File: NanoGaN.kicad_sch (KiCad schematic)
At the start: 19 parts, among them J1 XT60-M, J2 XT60-M, J3 Phase_U, J4 Phase_V, J5 Phase_W

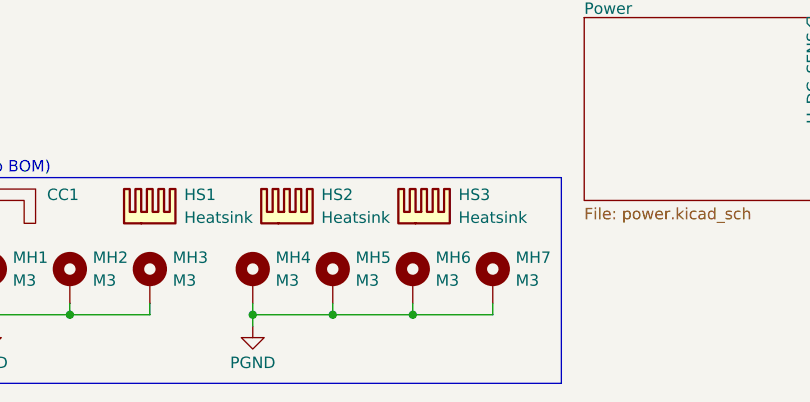
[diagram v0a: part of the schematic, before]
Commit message: new version of heatsink, channel and mounting holes
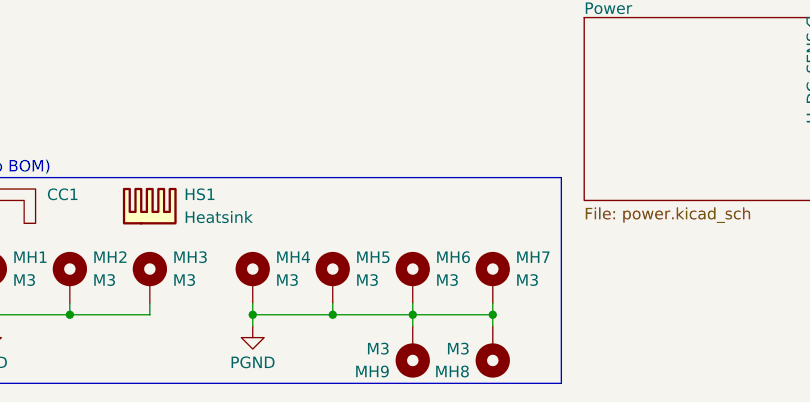
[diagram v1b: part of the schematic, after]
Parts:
- removed HS2, HS3: Heatsink, NanoGaN:HSB01-080808, symbol Mechanical:Heatsink
- added MH8, MH9: M3, MountingHole:MountingHole_3.2mm_M3_Pad_Via, symbol Mechanical:MountingHole_Pad
- HS1: footprint NanoGaN:HSB01-080808 -> NanoGaN:ICK_S
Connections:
- net PGND: now also MH8.1, MH9.1
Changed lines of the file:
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@@
+	)
+	(junction
+		(at 88.9 187.96)
+		(diameter 0)
+		(color 0 0 0 0)
 	)
 	(junction
@@
 	(wire
 		(pts
-			(xy 80.01 187.96) (xy 88.9 187.96)
-		)
-		(stroke
-			(width 0)
-			(type default)
-		)
-	)
-	(wire
-		(pts
 			(xy 88.9 54.61) (xy 99.06 54.61)
 		)
@@
 	(wire
 		(pts
+			(xy 88.9 187.96) (xy 80.01 187.96)
+		)
+		(stroke
+			(width 0)
+			(type default)
+		)
+	)
+	(wire
+		(pts
 			(xy 149.86 43.18) (xy 162.56 43.18)
 		)
@@
 	(wire
 		(pts
+			(xy 80.01 189.23) (xy 80.01 187.96)
+		)
+		(stroke
+			(width 0)
+			(type default)
+		)
+	)
+	(wire
+		(pts
 			(xy 88.9 24.13) (xy 99.06 24.13)
 		)
@@
 	(wire
 		(pts
+			(xy 88.9 189.23) (xy 88.9 187.96)
+		)
+		(stroke
+			(width 0)
+			(type default)
+		)
+	)
+	(wire
+		(pts
 			(xy 88.9 36.83) (xy 99.06 36.83)
 		)
@@
 			(width 0)
 			(type default)
+		)
+	)
+	(symbol
+		(lib_id "Mechanical:MountingHole_Pad")
+		(at 80.01 191.77 180)
+		(unit 1)
+		(exclude_from_sim yes)
+		(in_bom no)
+		(on_board yes)
+		(dnp no)
+		(fields_autoplaced yes)
+		(property "Reference" "MH9"
+			(at 77.47 194.3101 0)
+			(effects
+				(font
+					(size 1.27 1.27)
+				)
+				(justify left)
+			)
+		)
+		(property "Value" "M3"
+			(at 77.47 191.7701 0)
+			(effects
+				(font
+					(size 1.27 1.27)
+				)
+				(justify left)
+			)
+		)
+		(property "Footprint" "MountingHole:MountingHole_3.2mm_M3_Pad_Via"
+			(at 80.01 191.77 0)
+			(effects
+				(font
+					(size 1.27 1.27)
+				)
+				(hide yes)
+			)
+		)
+		(property "Datasheet" "~"
+			(at 80.01 191.77 0)
+			(effects
+				(font
+					(size 1.27 1.27)
+				)
+				(hide yes)
+			)
+		)
+		(property "Description" "Mounting Hole with connection"
+			(at 80.01 191.77 0)
+			(effects
+				(font
+					(size 1.27 1.27)
+				)
+				(hide yes)
+			)
+		)
+		(pin "1"
+		)
+		(instances
+			(project "NanoGaN"
+				(path "/aa8a494f-605e-4a00-9d3c-daec94709fcb"
+					(reference "MH9")
+					(unit 1)
+				)
+			)
 		)
 	)
@@
 	)
 	(symbol
-		(lib_id "Mechanical:Heatsink")
-		(at 66.04 177.8 0)
-		(unit 1)
-		(exclude_from_sim no)
-		(in_bom yes)
-		(on_board yes)
-		(dnp no)
-		(fields_autoplaced yes)
-		(property "Reference" "HS2"
-			(at 69.85 174.6249 0)
-			(effects
-				(font
-					(size 1.27 1.27)
-				)
-				(justify left)
-			)
-		)
-		(property "Value" "Heatsink"
-			(at 69.85 177.1649 0)
-			(effects
-				(font
-					(size 1.27 1.27)
-				)
-				(justify left)
-			)
-		)
-		(property "Footprint" "NanoGaN:HSB01-080808"
-			(at 66.3448 177.8 0)
-			(effects
-				(font
-					(size 1.27 1.27)
-				)
-				(hide yes)
-			)
-		)
-		(property "Datasheet" "~"
-			(at 66.3448 177.8 0)
-			(effects
-				(font
-					(size 1.27 1.27)
-				)
-				(hide yes)
-			)
-		)
-		(property "Description" "Heatsink"
-			(at 66.04 177.8 0)
-			(effects
-				(font
-					(size 1.27 1.27)
-				)
-				(hide yes)
-			)
-		)
-		(instances
-			(project "NanoGaN"
-				(path "/aa8a494f-605e-4a00-9d3c-daec94709fcb"
-					(reference "HS2")
-					(unit 1)
-				)
-			)
-		)
-	)
-	(symbol
-		(lib_id "Mechanical:Heatsink")
-		(at 81.28 177.8 0)
-		(unit 1)
-		(exclude_from_sim no)
-		(in_bom yes)
-		(on_board yes)
-		(dnp no)
-		(fields_autoplaced yes)
-		(property "Reference" "HS3"
-			(at 85.09 174.6249 0)
-			(effects
-				(font
-					(size 1.27 1.27)
-				)
-				(justify left)
-			)
-		)
-		(property "Value" "Heatsink"
-			(at 85.09 177.1649 0)
-			(effects
-				(font
-					(size 1.27 1.27)
-				)
-				(justify left)
-			)
-		)
-		(property "Footprint" "NanoGaN:HSB01-080808"
-			(at 81.5848 177.8 0)
-			(effects
-				(font
-					(size 1.27 1.27)
-				)
-				(hide yes)
-			)
-		)
-		(property "Datasheet" "~"
-			(at 81.5848 177.8 0)
-			(effects
-				(font
-					(size 1.27 1.27)
-				)
-				(hide yes)
-			)
-		)
-		(property "Description" "Heatsink"
-			(at 81.28 177.8 0)
-			(effects
-				(font
-					(size 1.27 1.27)
-				)
-				(hide yes)
-			)
-		)
-		(instances
-			(project "NanoGaN"
-				(path "/aa8a494f-605e-4a00-9d3c-daec94709fcb"
-					(reference "HS3")
-					(unit 1)
-				)
-			)
-		)
-	)
-	(symbol
 		(lib_id "Mechanical:MountingHole_Pad")
 		(at 62.23 184.15 0)
@@
 	)
 	(symbol
+		(lib_id "Mechanical:MountingHole_Pad")
+		(at 88.9 191.77 180)
+		(unit 1)
+		(exclude_from_sim yes)
+		(in_bom no)
+		(on_board yes)
+		(dnp no)
+		(fields_autoplaced yes)
+		(property "Reference" "MH8"
+			(at 86.36 194.3101 0)
+			(effects
+				(font
+					(size 1.27 1.27)
+				)
+				(justify left)
+			)
+		)
+		(property "Value" "M3"
+			(at 86.36 191.7701 0)
+			(effects
+				(font
+					(size 1.27 1.27)
+				)
+				(justify left)
+			)
+		)
+		(property "Footprint" "MountingHole:MountingHole_3.2mm_M3_Pad_Via"
+			(at 88.9 191.77 0)
+			(effects
+				(font
+					(size 1.27 1.27)
+				)
+				(hide yes)
+			)
+		)
+		(property "Datasheet" "~"
+			(at 88.9 191.77 0)
+			(effects
+				(font
+					(size 1.27 1.27)
+				)
+				(hide yes)
+			)
+		)
+		(property "Description" "Mounting Hole with connection"
+			(at 88.9 191.77 0)
+			(effects
+				(font
+					(size 1.27 1.27)
+				)
+				(hide yes)
+			)
+		)
+		(pin "1"
+		)
+		(instances
+			(project "NanoGaN"
+				(path "/aa8a494f-605e-4a00-9d3c-daec94709fcb"
+					(reference "MH8")
+					(unit 1)
+				)
+			)
+		)
+	)
+	(symbol
 		(lib_id "power:GND")
 		(at 33.02 189.23 0)
@@
 		(on_board yes)
 		(dnp no)
-		(fields_autoplaced yes)
 		(property "Reference" "HS1"
 			(at 54.61 174.6249 0)
@@
 			)
 		)
-		(property "Footprint" "NanoGaN:HSB01-080808"
-			(at 51.1048 177.8 0)
-			(effects
-				(font
+		(property "Footprint" "NanoGaN:ICK_S"
+			(at 74.676 177.292 0)
+			(effects
+				(font

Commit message: wip layout
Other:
- moved on the sheet: J1, J2
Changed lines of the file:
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@@
 	)
 	(junction
-		(at 248.92 85.09)
+		(at 247.65 67.31)
 		(diameter 0)
 		(color 0 0 0 0)
@@
 	)
 	(junction
-		(at 248.92 88.9)
+		(at 247.65 71.12)
 		(diameter 0)
 		(color 0 0 0 0)
@@
 	(wire
 		(pts
-			(xy 248.92 88.9) (xy 250.19 88.9)
+			(xy 247.65 71.12) (xy 248.92 71.12)
 		)
 		(stroke
@@
 	(wire
 		(pts
-			(xy 248.92 81.28) (xy 248.92 85.09)
+			(xy 247.65 63.5) (xy 247.65 67.31)
 		)
 		(stroke
@@
 	(wire
 		(pts
-			(xy 248.92 93.98) (xy 248.92 88.9)
+			(xy 247.65 76.2) (xy 247.65 71.12)
 		)
 		(stroke
@@
 	(wire
 		(pts
-			(xy 248.92 85.09) (xy 250.19 85.09)
+			(xy 247.65 67.31) (xy 248.92 67.31)
 		)
 		(stroke
@@
 	(symbol
 		(lib_id "power:GND")
-		(at 248.92 93.98 0)
+		(at 247.65 76.2 0)
 		(unit 1)
 		(exclude_from_sim no)
@@
 		(dnp no)
 		(property "Reference" "#PWR068"
-			(at 248.92 100.33 0)
+			(at 247.65 82.55 0)
 			(effects
 				(font
@@
 		)
 		(property "Value" "PGND"
-			(at 248.92 97.79 0)
+			(at 247.65 80.01 0)
 			(effects
 				(font
@@
 		)
 		(property "Footprint" ""
-			(at 248.92 93.98 0)
+			(at 247.65 76.2 0)
 			(effects
 				(font
@@
 		)
 		(property "Datasheet" ""
-			(at 248.92 93.98 0)
+			(at 247.65 76.2 0)
 			(effects
 				(font
@@
 		)
 		(property "Description" ""
-			(at 248.92 93.98 0)
+			(at 247.65 76.2 0)
 			(effects
 				(font
@@
 	(symbol
 		(lib_id "power:VDC")
-		(at 248.92 81.28 0)
+		(at 247.65 63.5 0)
 		(unit 1)
 		(exclude_from_sim no)
@@
 		(dnp no)
 		(property "Reference" "#PWR067"
-			(at 248.92 83.82 0)
+			(at 247.65 66.04 0)
 			(effects
 				(font
@@
 		)
 		(property "Value" "U_DC"
-			(at 246.38 77.47 0)
+			(at 245.11 59.69 0)
 			(effects
 				(font
@@
 		)
 		(property "Footprint" ""
-			(at 248.92 81.28 0)
+			(at 247.65 63.5 0)
 			(effects
 				(font
@@
 		)
 		(property "Datasheet" ""
-			(at 248.92 81.28 0)
+			(at 247.65 63.5 0)
 			(effects
 				(font
@@
 		)
 		(property "Description" ""
-			(at 248.92 81.28 0)
+			(at 247.65 63.5 0)
 			(effects
 				(font
@@
 	(symbol
 		(lib_id "NanoGaN:XT60-M")
-		(at 255.27 83.82 0)
+		(at 254 66.04 0)
 		(unit 1)
 		(exclude_from_sim no)
@@
 		(dnp no)
 		(property "Reference" "J1"
-			(at 255.016 82.804 0)
+			(at 253.746 65.024 0)
 			(effects
 				(font
@@
 		)
 		(property "Value" "XT60-M"
-			(at 255.27 92.964 0)
+			(at 254 75.184 0)
 			(effects
 				(font
@@
 		)
 		(property "Footprint" "NanoGaN:AMASS_XT60-M"
-			(at 256.54 100.838 0)
+			(at 255.27 83.058 0)
 			(effects
 				(font
@@
 		)
 		(property "Datasheet" ""
-			(at 255.27 83.82 0)
+			(at 254 66.04 0)
 			(effects
 				(font
@@
 		)
 		(property "Description" "Plug; DC supply; XT60; male; PIN: 2; for cable; soldered; 30A; 500V"
-			(at 259.842 98.044 0)
+			(at 258.572 80.264 0)
 			(effects
 				(font
@@
 		)
 		(property "MAXIMUM_PACKAGE_HEIGHT" "16.00 mm"
-			(at 250.952 103.124 0)
+			(at 249.682 85.344 0)
 			(effects
 				(font
@@
 		)
 		(property "Package" "Package"
-			(at 274.828 101.854 0)
+			(at 273.558 84.074 0)
 			(effects
 				(font
@@
 		)
 		(property "MP" "XT60-M"
-			(at 251.714 101.6 0)
+			(at 250.444 83.82 0)
 			(effects
 				(font
@@
 	(symbol
 		(lib_id "NanoGaN:XT60-M")
-		(at 243.84 83.82 0)
+		(at 242.57 66.04 0)
 		(mirror y)
 		(unit 1)
@@
 		(dnp no)
 		(property "Reference" "J2"
-			(at 244.094 82.804 0)
+			(at 242.824 65.024 0)
 			(effects
 				(font
@@
 		)
 		(property "Value" "XT60-M"
-			(at 243.84 92.964 0)
+			(at 242.57 75.184 0)
 			(effects
 				(font
@@
 		)
 		(property "Footprint" "NanoGaN:AMASS_XT60-M"
-			(at 242.57 100.838 0)
+			(at 241.3 83.058 0)
 			(effects
 				(font
@@
 		)
 		(property "Datasheet" ""
-			(at 243.84 83.82 0)
+			(at 242.57 66.04 0)
 			(effects
 				(font
@@
 		)
 		(property "Description" "Plug; DC supply; XT60; male; PIN: 2; for cable; soldered; 30A; 500V"
-			(at 239.268 98.044 0)
+			(at 237.998 80.264 0)
 			(effects
 				(font
@@
 		)
 		(property "MAXIMUM_PACKAGE_HEIGHT" "16.00 mm"
-			(at 248.158 103.124 0)
+			(at 246.888 85.344 0)
 			(effects
 				(font
@@
 		)
 		(property "Package" "Package"
-			(at 224.282 101.854 0)
+			(at 223.012 84.074 0)
 			(effects
 				(font
@@
 		)
 		(property "MP" "XT60-M"
-			(at 247.396 101.6 0)
-			(effects
-				(font
+			(at 246.126 83.82 0)
+			(effects
+				(font

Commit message: wip layout
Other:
- sheet HalfBridgeU ports: added GATE+, GATE-; removed HI, LI
- sheet HalfBridgeV ports: added GATE+, GATE-; removed HI, LI
- sheet HalfBridgeW ports: added GATE+, GATE-; removed HI, LI
- sheet MCU ports: added GATE_U+, GATE_U-, GATE_V+, GATE_V-, GATE_W+, GATE_W-, UART4_RX, UART4_TX; removed GATE_U_HI, GATE_U_LI, GATE_V_HI, GATE_V_LI, GATE_W_HI, GATE_W_LI, USART1_RX, USART1_TX
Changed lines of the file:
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@@
-			)
-		)
-		(pin "HI" input
-			(at 162.56 68.58 180)
-			(effects
-				(font
-					(size 1.27 1.27)
-				)
-				(justify left)
-			)
-		)
-		(pin "LI" input
-			(at 162.56 72.39 180)
-			(effects
-				(font
-					(size 1.27 1.27)
-				)
-				(justify left)
 			)
 		)
@@
 		(pin "I_CURR_SENS-" output
 			(at 162.56 83.82 180)
+			(effects
+				(font
+					(size 1.27 1.27)
+				)
+				(justify left)
+			)
+		)
+		(pin "GATE-" input
+			(at 162.56 72.39 180)
+			(effects
+				(font
+					(size 1.27 1.27)
+				)
+				(justify left)
+			)
+		)
+		(pin "GATE+" input
+			(at 162.56 68.58 180)
 			(effects
 				(font
@@
 			)
 		)
-		(pin "HI" input
-			(at 162.56 24.13 180)
-			(effects
-				(font
-					(size 1.27 1.27)
-				)
-				(justify left)
-			)
-		)
-		(pin "LI" input
-			(at 162.56 27.94 180)
-			(effects
-				(font
-					(size 1.27 1.27)
-				)
-				(justify left)
-			)
-		)
 		(pin "PHASE" bidirectional
 			(at 189.23 40.64 0)
@@
 		(pin "I_CURR_SENS-" output
 			(at 162.56 39.37 180)
+			(effects
+				(font
+					(size 1.27 1.27)
+				)
+				(justify left)
+			)
+		)
+		(pin "GATE-" input
+			(at 162.56 27.94 180)
+			(effects
+				(font
+					(size 1.27 1.27)
+				)
+				(justify left)
+			)
+		)
+		(pin "GATE+" input
+			(at 162.56 24.13 180)
 			(effects
 				(font
@@
 			)
 		)
-		(pin "USART1_TX" output
-			(at 99.06 34.29 180)
-			(effects
-				(font
-					(size 1.27 1.27)
-				)
-				(justify left)
-			)
-		)
-		(pin "USART1_RX" input
-			(at 99.06 36.83 180)
-			(effects
-				(font
-					(size 1.27 1.27)
-				)
-				(justify left)
-			)
-		)
 		(pin "SWO" output
 			(at 99.06 31.75 180)
@@
 			)
 		)
-		(pin "GATE_V_LI" output
-			(at 149.86 72.39 0)
-			(effects
-				(font
-					(size 1.27 1.27)
-				)
-				(justify right)
-			)
-		)
-		(pin "GATE_V_HI" output
-			(at 149.86 68.58 0)
-			(effects
-				(font
-					(size 1.27 1.27)
-				)
-				(justify right)
-			)
-		)
-		(pin "GATE_W_LI" output
-			(at 149.86 116.84 0)
-			(effects
-				(font
-					(size 1.27 1.27)
-				)
-				(justify right)
-			)
-		)
-		(pin "GATE_U_LI" output
-			(at 149.86 27.94 0)
-			(effects
-				(font
-					(size 1.27 1.27)
-				)
-				(justify right)
-			)
-		)
-		(pin "GATE_W_HI" output
-			(at 149.86 113.03 0)
-			(effects
-				(font
-					(size 1.27 1.27)
-				)
-				(justify right)
-			)
-		)
-		(pin "GATE_U_HI" output
-			(at 149.86 24.13 0)
-			(effects
-				(font
-					(size 1.27 1.27)
-				)
-				(justify right)
-			)
-		)
 		(pin "EXT_TEMP2" input
 			(at 99.06 41.91 180)
@@
 				)
 				(justify right)
+			)
+		)
+		(pin "GATE_W+" output
+			(at 149.86 113.03 0)
+			(effects
+				(font
+					(size 1.27 1.27)
+				)
+				(justify right)
+			)
+		)
+		(pin "GATE_V-" output
+			(at 149.86 72.39 0)
+			(effects
+				(font
+					(size 1.27 1.27)
+				)
+				(justify right)
+			)
+		)
+		(pin "GATE_V+" output
+			(at 149.86 68.58 0)
+			(effects
+				(font
+					(size 1.27 1.27)
+				)
+				(justify right)
+			)
+		)
+		(pin "GATE_U-" output
+			(at 149.86 27.94 0)
+			(effects
+				(font
+					(size 1.27 1.27)
+				)
+				(justify right)
+			)
+		)
+		(pin "GATE_U+" output
+			(at 149.86 24.13 0)
+			(effects
+				(font
+					(size 1.27 1.27)
+				)
+				(justify right)
+			)
+		)
+		(pin "GATE_W-" output
+			(at 149.86 116.84 0)
+			(effects
+				(font
+					(size 1.27 1.27)
+				)
+				(justify right)
+			)
+		)
+		(pin "UART4_TX" output
+			(at 99.06 34.29 180)
+			(effects
+				(font
+					(size 1.27 1.27)
+				)
+				(justify left)
+			)
+		)
+		(pin "UART4_RX" input
+			(at 99.06 36.83 180)
+			(effects
+				(font
+					(size 1.27 1.27)
+				)
+				(justify left)
 			)
 		)
@@
 			)
 		)
-		(pin "HI" input
-			(at 162.56 113.03 180)
-			(effects
-				(font
-					(size 1.27 1.27)
-				)
-				(justify left)
-			)
-		)
-		(pin "LI" input
-			(at 162.56 116.84 180)
-			(effects
-				(font
-					(size 1.27 1.27)
-				)
-				(justify left)
-			)
-		)
 		(pin "PHASE" bidirectional
 			(at 189.23 129.54 0)
@@
 			(effects
 				(font
+					(size 1.27 1.27)
+				)
+				(justify left)
+			)
+		)
+		(pin "GATE-" input
+			(at 162.56 116.84 180)
+			(effects
+				(font
+					(size 1.27 1.27)
+				)
+				(justify left)
+			)
+		)
+		(pin "GATE+" input
+			(at 162.56 113.03 180)
+			(effects
+				(font

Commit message: first draft of the PCB
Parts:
- added FM4: Fiducial, Fiducial:Fiducial_1mm_Mask2mm, symbol Mechanical:Fiducial
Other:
- moved on the sheet: FM1, FM2, FM3
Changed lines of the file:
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@@
 	(symbol
 		(lib_id "Mechanical:Fiducial")
-		(at 17.78 185.42 0)
+		(at 17.78 182.88 0)
 		(unit 1)
 		(exclude_from_sim yes)
@@
 		(fields_autoplaced yes)
 		(property "Reference" "FM2"
+			(at 20.32 181.6099 0)
+			(effects
+				(font
+					(size 1.27 1.27)
+				)
+				(justify left)
+			)
+		)
+		(property "Value" "Fiducial"
 			(at 20.32 184.1499 0)
 			(effects
@@
 			)
 		)
-		(property "Value" "Fiducial"
-			(at 20.32 186.6899 0)
-			(effects
-				(font
-					(size 1.27 1.27)
-				)
-				(justify left)
-			)
-		)
 		(property "Footprint" "Fiducial:Fiducial_1mm_Mask2mm"
-			(at 17.78 185.42 0)
+			(at 17.78 182.88 0)
 			(effects
 				(font
@@
 		)
 		(property "Datasheet" "~"
-			(at 17.78 185.42 0)
+			(at 17.78 182.88 0)
 			(effects
 				(font
@@
 		)
 		(property "Description" "Fiducial Marker"
-			(at 17.78 185.42 0)
+			(at 17.78 182.88 0)
 			(effects
 				(font
@@
 	(symbol
 		(lib_id "Mechanical:Fiducial")
-		(at 17.78 190.5 0)
+		(at 17.78 187.96 0)
 		(unit 1)
 		(exclude_from_sim yes)
@@
 		(fields_autoplaced yes)
 		(property "Reference" "FM3"
+			(at 20.32 186.6899 0)
+			(effects
+				(font
+					(size 1.27 1.27)
+				)
+				(justify left)
+			)
+		)
+		(property "Value" "Fiducial"
 			(at 20.32 189.2299 0)
 			(effects
@@
 			)
 		)
-		(property "Value" "Fiducial"
-			(at 20.32 191.7699 0)
-			(effects
-				(font
-					(size 1.27 1.27)
-				)
-				(justify left)
-			)
-		)
 		(property "Footprint" "Fiducial:Fiducial_1mm_Mask2mm"
-			(at 17.78 190.5 0)
+			(at 17.78 187.96 0)
 			(effects
 				(font
@@
 		)
 		(property "Datasheet" "~"
-			(at 17.78 190.5 0)
+			(at 17.78 187.96 0)
 			(effects
 				(font
@@
 		)
 		(property "Description" "Fiducial Marker"
-			(at 17.78 190.5 0)
+			(at 17.78 187.96 0)
 			(effects
 				(font
@@
 	(symbol
 		(lib_id "Mechanical:Fiducial")
-		(at 17.78 180.34 0)
+		(at 17.78 177.8 0)
 		(unit 1)
 		(exclude_from_sim yes)
@@
 		(fields_autoplaced yes)
 		(property "Reference" "FM1"
+			(at 20.32 176.5299 0)
+			(effects
+				(font
+					(size 1.27 1.27)
+				)
+				(justify left)
+			)
+		)
+		(property "Value" "Fiducial"
 			(at 20.32 179.0699 0)
 			(effects
@@
 			)
 		)
-		(property "Value" "Fiducial"
-			(at 20.32 181.6099 0)
-			(effects
-				(font
-					(size 1.27 1.27)
-				)
-				(justify left)
-			)
-		)
 		(property "Footprint" "Fiducial:Fiducial_1mm_Mask2mm"
-			(at 17.78 180.34 0)
+			(at 17.78 177.8 0)
 			(effects
 				(font
@@
 		)
 		(property "Datasheet" "~"
-			(at 17.78 180.34 0)
+			(at 17.78 177.8 0)
 			(effects
 				(font
@@
 		)
 		(property "Description" "Fiducial Marker"
-			(at 17.78 180.34 0)
+			(at 17.78 177.8 0)
 			(effects
 				(font
@@
 					(unit 1)
 				)
+			)
+		)
+	)
+	(symbol
+		(lib_id "Mechanical:Fiducial")
+		(at 17.78 193.04 0)
+		(unit 1)
+		(exclude_from_sim yes)
+		(in_bom no)
+		(on_board yes)
+		(dnp no)
+		(fields_autoplaced yes)
+		(property "Reference" "FM4"
+			(at 20.32 191.7699 0)
+			(effects
+				(font
+					(size 1.27 1.27)
+				)
+				(justify left)
+			)
+		)
+		(property "Value" "Fiducial"
+			(at 20.32 194.3099 0)
+			(effects
+				(font
+					(size 1.27 1.27)
+				)
+				(justify left)
+			)
+		)
+		(property "Footprint" "Fiducial:Fiducial_1mm_Mask2mm"
+			(at 17.78 193.04 0)
+			(effects
+				(font
+					(size 1.27 1.27)
+				)
+				(hide yes)
+			)
+		)
+		(property "Datasheet" "~"
+			(at 17.78 193.04 0)
+			(effects
+				(font
+					(size 1.27 1.27)
+				)
+				(hide yes)
+			)
+		)
+		(property "Description" "Fiducial Marker"
+			(at 17.78 193.04 0)
+			(effects
+				(font
+					(size 1.27 1.27)
+				)
+				(hide yes)
+			)
+		)
+		(instances
+			(project "NanoGaN"
+				(path "/aa8a494f-605e-4a00-9d3c-daec94709fcb"
+					(reference "FM4")
+					(unit 1)
+				)
